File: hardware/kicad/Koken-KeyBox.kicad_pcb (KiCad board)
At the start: 2 copper layers, 30.5 x 65.1 mm, 8 parts, among them J1 Jack-DC, J2 LED, J3 Servo

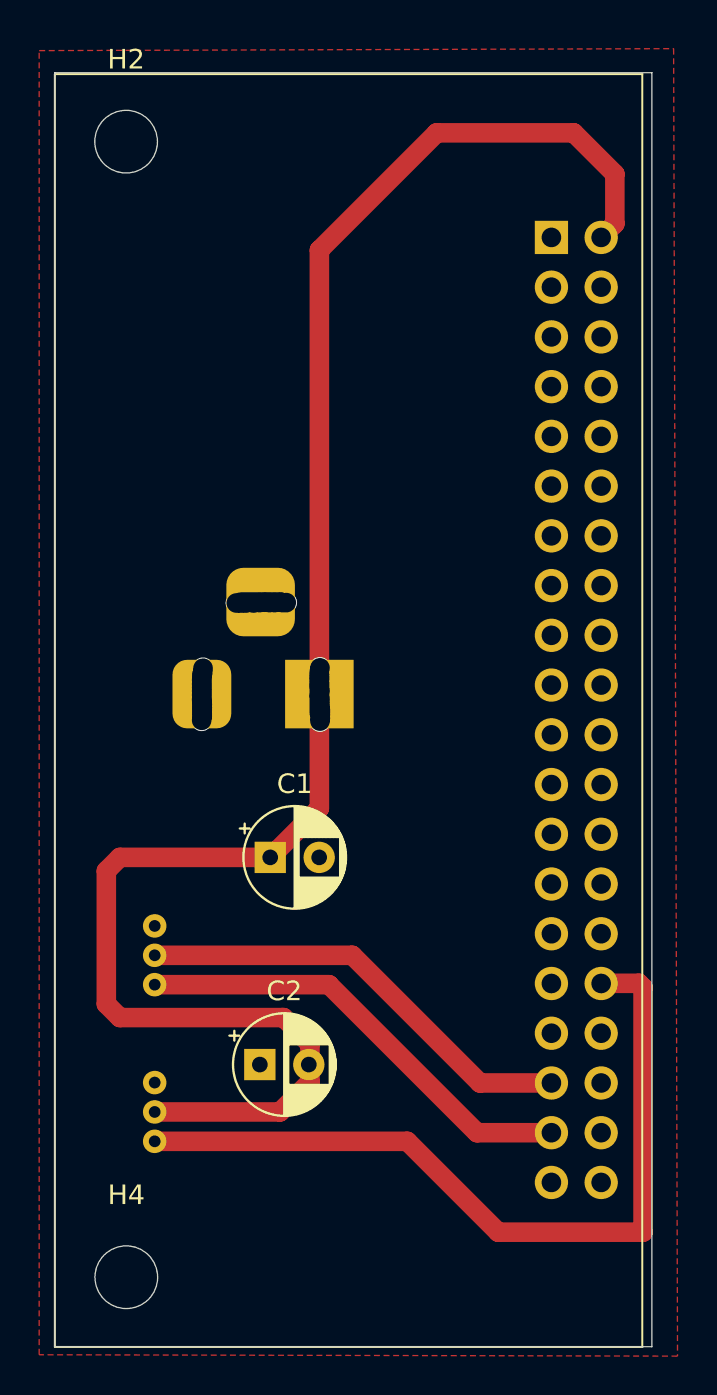
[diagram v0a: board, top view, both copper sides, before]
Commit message: コネクタをXHに、電源用コネクタをType-Cに変更
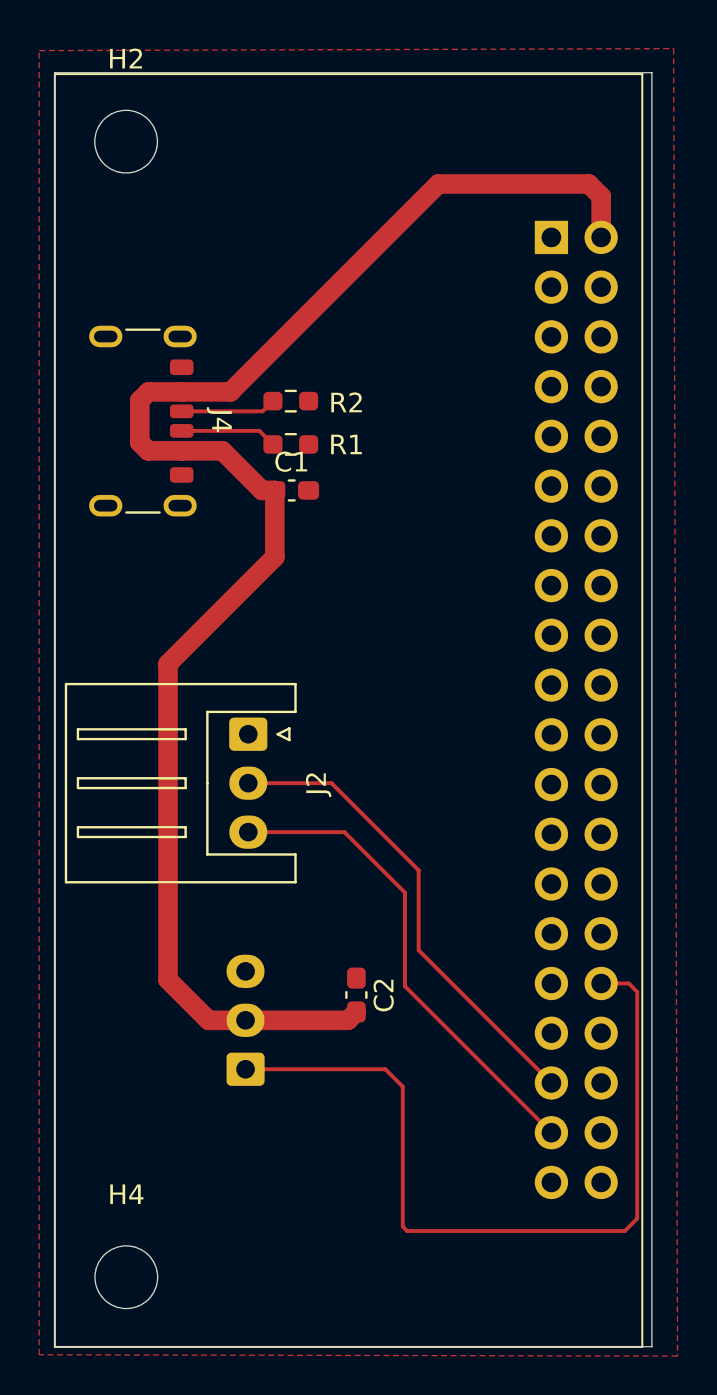
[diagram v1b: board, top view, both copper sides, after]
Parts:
- removed J1: Jack-DC, Connector_BarrelJack:BarrelJack_Horizontal
- added J4: USB_C_Receptacle_PowerOnly_6P, Connector_USB:USB_C_Receptacle_GCT_USB4125-xx-x_6P_TopMnt_Horizontal, F.Cu at (127.9, 62.7)
- added R1: 5.1k, Resistor_SMD:R_0603_1608Metric_Pad0.98x0.95mm_HandSolder, F.Cu at (136.6, 63.9)
- added R2: 5.1k, Resistor_SMD:R_0603_1608Metric_Pad0.98x0.95mm_HandSolder, F.Cu at (136.6, 61.7)
- C1, C2: footprint Capacitor_THT:CP_Radial_D5.0mm_P2.50mm -> Capacitor_SMD:C_0603_1608Metric_Pad1.08x0.95mm_HandSolder
- J2: footprint MyLibrary:ZH_3P_Side -> Connector_JST:JST_XH_S3B-XH-A_1x03_P2.50mm_Horizontal; moved to F.Cu
- J3: footprint MyLibrary:ZH_3P_Side -> Connector_JST:JST_XH_S3B-XH-A_1x03_P2.50mm_Horizontal
- moved C1 18.8 mm to (136.6, 66.3)
- moved J2 13.0 mm to (134.4, 78.7), turned to -90 degrees
- moved J3 6.61 mm to (134.2, 95.8)
- moved C2 6.08 mm to (139.9, 92.0), turned to -90 degrees
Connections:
- J2 pad 1: LED_Failure -> GND
- J2 pad 3: GND -> LED_Failure
- U1 pad 20: unconnected-(U1-GND-Pad20) -> GND
- U1 pad 25: unconnected-(U1-GND-Pad25) -> GND
- U1 pad 39: unconnected-(U1-GND-Pad39) -> GND
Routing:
- net +5V: track 91.2 -> 78.5 mm, vias 18 -> 0
- net Net-(J4-CC2): track 0.00 -> 4.94 mm
- net Net-(J4-CC1): track 0.00 -> 4.87 mm
- net LED_Success: track 23.0 -> 24.2 mm
- net LED_Failure: track 23.4 -> 24.6 mm
- net GND: vias 16 -> 0
- net (no net): vias 11 -> 0
